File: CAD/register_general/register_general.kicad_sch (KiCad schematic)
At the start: 41 parts, among them J1 Conn_01x16_Pin, J2 Conn_01x16_Pin, U1 74HC245, U2 74HC377

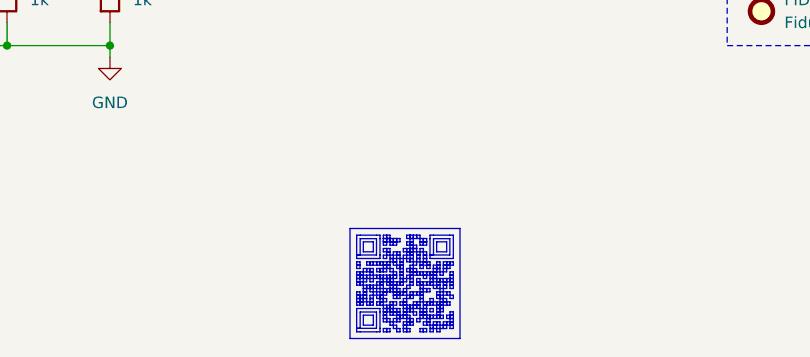
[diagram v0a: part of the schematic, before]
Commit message: update KiCAD version 10.0
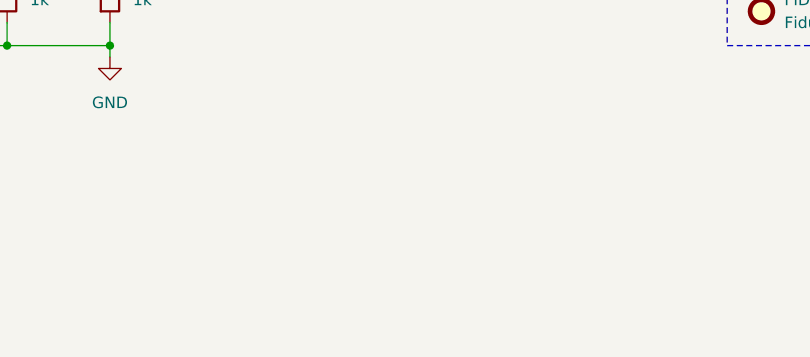
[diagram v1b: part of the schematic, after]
